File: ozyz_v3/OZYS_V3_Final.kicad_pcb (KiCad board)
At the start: 4 copper layers, 56 x 69 mm, 113 parts, among them CN1 532610571, J2 Conn_01x02_Pin, J3 AudioJack4, J4 AudioJack4, J5 AudioJack4, J6 AudioJack4, Q1 AO3400A, Q2 AO3401A, U1 ISO1044BD, U10 FTC252012S1R5MBCA (1.5uF 2.9A)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

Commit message: Ozys finalized?
Hopefully
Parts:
- moved U7 3.35 mm to (50.3, 63.9)
- moved U9 0.91 mm to (50.3, 70.8)
- moved LED5 0.87 mm to (52.1, 44.8)
- moved R1 0.87 mm to (52.1, 47.7)
- moved U6 0.60 mm to (46.8, 70.8)
- moved U11 0.40 mm to (57.3, 27.7)
- moved R9 0.22 mm to (71.6, 31.8)
- moved R10 0.10 mm to (72.7, 31.8)
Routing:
- net Net-(D2-K): track 11.0 -> 0.00 mm
- net /LED2: track 45.1 -> 34.2 mm
- net GND: track 107.4 -> 98.6 mm, vias 44 -> 48
- net /3V3A_SW_EN: track 19.3 -> 16.3 mm, vias 4 -> 2
- net /DM1: track 46.0 -> 47.8 mm
- net /USB_DN: track 34.5 -> 36.2 mm
- net 3V3A_SW: track 63.5 -> 61.8 mm
- net /USB_DP: track 36.2 -> 37.8 mm
- net /ONE_WIRE_OUT2: track 46.7 -> 45.4 mm
- net /CAN_RXD: track 49.4 -> 50.4 mm
- net /STATUS_LED: track 6.20 -> 7.11 mm
- net /ONE_WIRE_OUT1: track 58.4 -> 57.6 mm
- net /DP2: track 23.6 -> 22.8 mm
- net /CS: track 41.6 -> 42.3 mm
- net /nRST: track 45.0 -> 45.7 mm
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- added copper zone on B.Cu, net GND
- added copper zone on B.Cu, net Net-(D2-K)

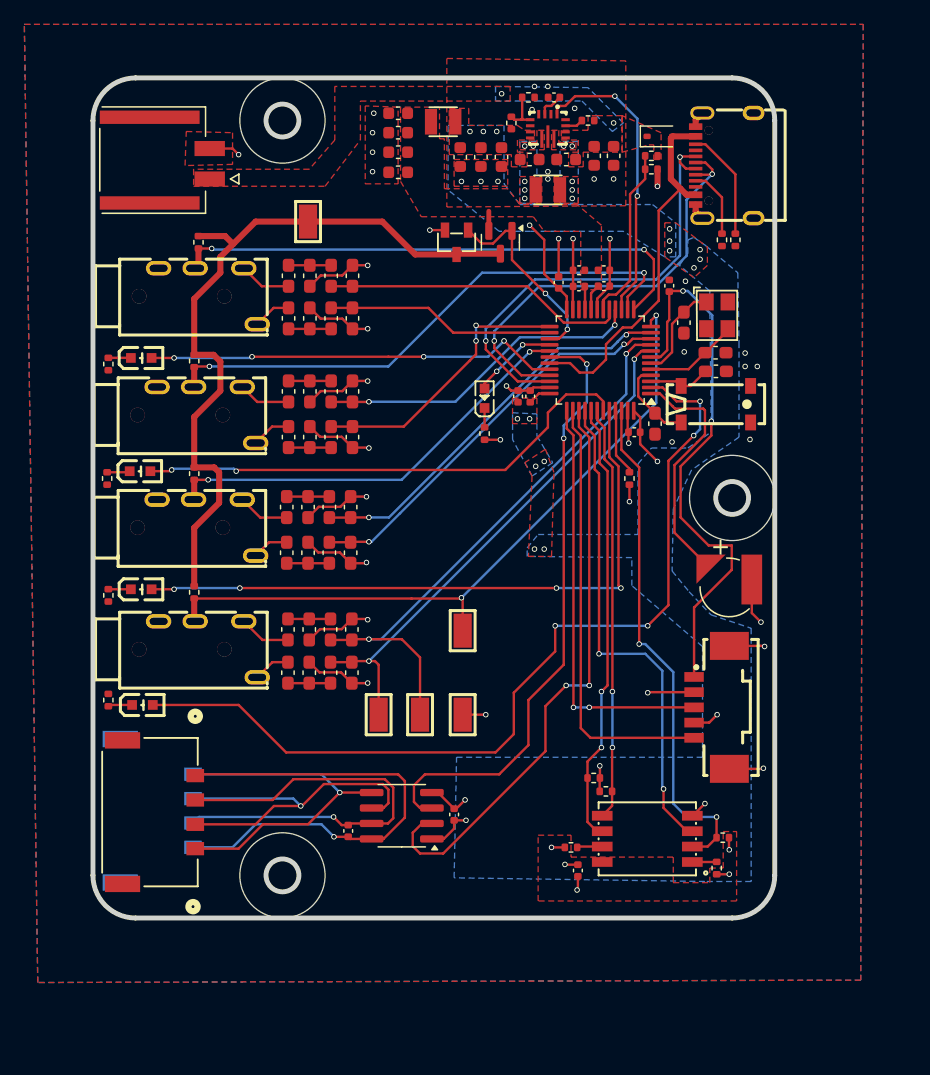
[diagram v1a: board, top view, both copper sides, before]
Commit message: Pours fixed, no Graphics
Made sure all pours conform to 8mils clearance and width, with Solid connections.
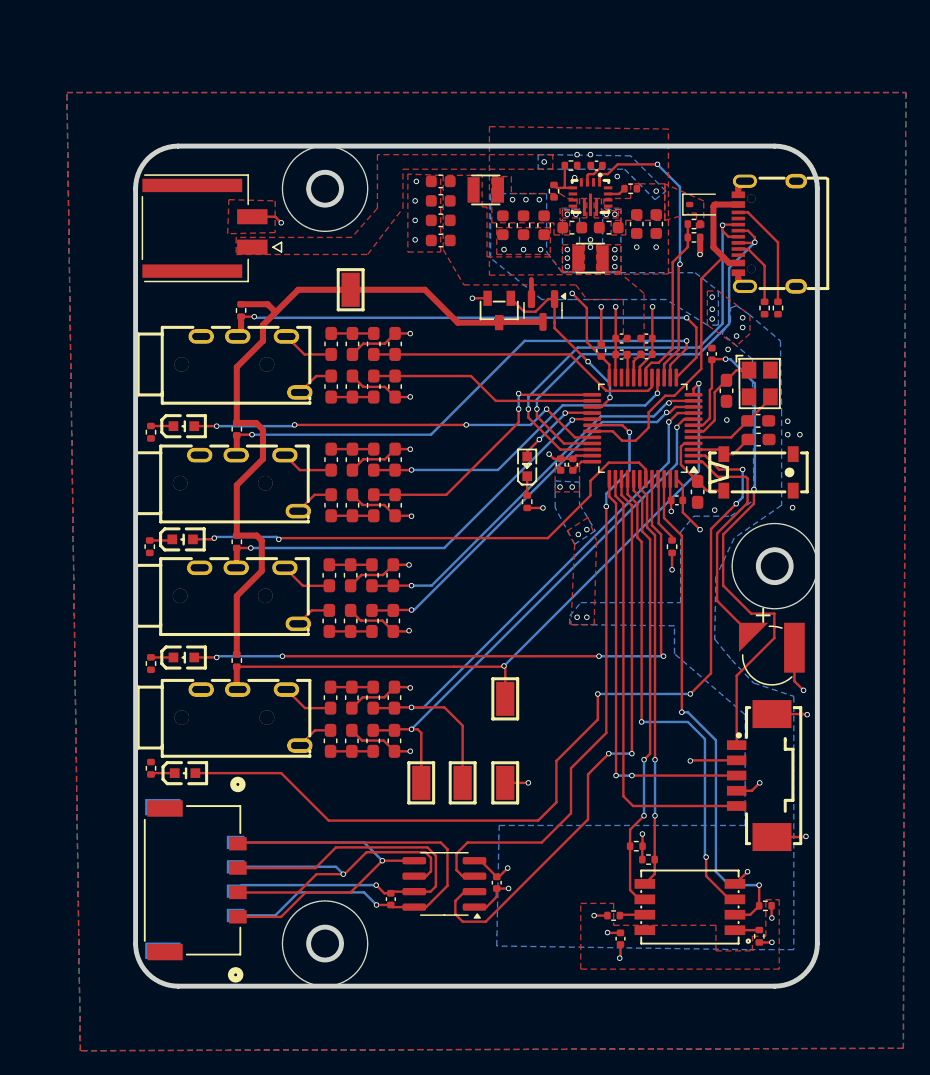
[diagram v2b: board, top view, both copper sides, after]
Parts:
- moved C13 6.60 mm to (63.3, 89.2)
- moved C2 6.60 mm to (44.7, 69.4)
- moved C3 6.60 mm to (44.4, 86.0)
- moved C30 6.60 mm to (41.2, 69.4)
- moved C34 6.60 mm to (41.2, 73.0)
- moved C7 6.60 mm to (44.7, 73.0)
- moved J_CAN2 6.60 mm to (27.9, 84.3)
- moved R13 6.60 mm to (43.0, 69.4)
- moved R14 6.60 mm to (43.0, 73.0)
- moved R15 6.60 mm to (24.7, 75.2)
- moved R19 6.60 mm to (39.5, 73.0)
- moved R28 6.60 mm to (39.5, 69.4)
- moved R3 6.60 mm to (65.6, 82.7)
- moved U1 6.60 mm to (48.8, 84.7)
- moved U5 6.60 mm to (46.9, 76.4)
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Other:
- outline, holes or cut-outs redrawn

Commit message: final touches
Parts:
- added G***: LOGO, Rocketry_Manual:OZYS_V3_ART, F.Cu at (51.5, 58.6)
- added G***: LOGO, Rocketry_Manual:OZYS_V3_LOGO, F.Cu at (46.9, 82.5)
- moved U7 35.1 mm to (44.6, 35.7), turned to 0 degrees
- moved U5 1.88 mm to (45.2, 77.1), turned to 0 degrees
- moved CN1 1.33 mm to (75.6, 75.8)
- moved U8 1.15 mm to (40.0, 35.7), turned to 0 degrees
- moved U9 0.97 mm to (54.5, 77.1), turned to 180 degrees
- moved U6 0.87 mm to (49.8, 77.1), turned to 180 degrees
- moved J2 0.28 mm to (29.0, 30.9)
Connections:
- U7 pad 1: /ONE_WIRE_OUT1 -> /ONE_WIRE_OUT3
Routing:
- net GND: track 98.6 -> 88.2 mm, vias 48 -> 149
- net 3V3A_SW: track 61.8 -> 64.6 mm
- net /ONE_WIRE_OUT1: track 57.6 -> 54.8 mm
- net /ONE_WIRE_OUT3: track 44.3 -> 46.8 mm, vias 2 -> 3
- net /DM1: track 47.8 -> 46.3 mm
- net /SWDIO: track 34.5 -> 35.8 mm
- net /SWDCLK: track 36.0 -> 37.3 mm
- net +3V3: track 27.6 -> 27.0 mm
- net Net-(J_CAN1-Pin_1): track 39.9 -> 39.3 mm
- net /nRST: track 45.7 -> 46.3 mm
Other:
- outline, holes or cut-outs redrawn

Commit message: Graphics Added on back
Yipiee
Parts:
- removed the G*** at (51.5, 58.6)
- added G***: LOGO, Rocketry_Manual:OZYS_V3_LOGO2, B.Cu at (51.9, 59.2)
- G***: moved to B.Cu
- moved G*** 17.5 mm to (64.1, 86.1), turned to 180 degrees

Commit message: Updated edge alignment and text
Yipeee
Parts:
- removed the G*** at (51.9, 59.2)
- added G***: LOGO, Rocketry_Manual:OZYS_V3_ART, B.Cu at (51.7, 58.5)
- moved R10 12.2 mm to (73.5, 25.5), turned to 0 degrees
- moved U9 5.71 mm to (54.5, 71.4)
- moved USB1 1.00 mm to (74.3, 31.3)
- moved J_CAN1 0.99 mm to (27.5, 83.6)
- moved J_CAN2 0.82 mm to (27.5, 83.6)
- moved D2 0.70 mm to (69.3, 28.9)
- moved R8 0.67 mm to (68.7, 30.8)
- moved R7 0.67 mm to (68.7, 31.9)
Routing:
- net GND: track 88.2 -> 84.1 mm
- net Net-(USB1-CC2): track 9.16 -> 6.01 mm
- net Net-(J_CAN1-Pin_1): track 39.3 -> 40.5 mm
- net Net-(J_CAN1-Pin_4): track 29.1 -> 30.3 mm
- net /USB_DN: track 36.2 -> 37.3 mm
- net Net-(USB1-CC1): track 5.70 -> 6.70 mm
- net Net-(J_CAN1-Pin_3): track 29.1 -> 30.1 mm
- net Net-(J_CAN1-Pin_2): track 36.9 -> 37.7 mm
- net /VBUS: track 31.1 -> 30.5 mm
- net /BAT_V_M: track 14.4 -> 13.8 mm
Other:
- board text added: "3V3A_SW"
- board text added: "DM"
- board text added: "DP"
- board text added: "GND"
- board text added: "ONE_WIRE_OUT"

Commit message: final touches
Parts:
- LED5: value 19-213/Y2C-CQ2R2L/3T(CY) -> 17-21SUYC/TR8; footprint Rocketry_Easyeda:LED0603-RD-YELLOW -> Rocketry_Easyeda:LED0805-R-RD
- moved R1 0.69 mm to (55.6, 54.0)
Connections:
- LED5 pad 1: Net-(LED5-C) -> /STATUS_LED
- LED5 pad 2: /STATUS_LED -> Net-(LED5--)
- R1 pad 1: Net-(LED5-C) -> Net-(LED5--)
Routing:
- net Net-(LED5--): track 0.00 -> 2.04 mm
- net Net-(LED5-C): track 1.59 -> 0.00 mm
- net GND: track 84.1 -> 82.8 mm, vias 149 -> 150
